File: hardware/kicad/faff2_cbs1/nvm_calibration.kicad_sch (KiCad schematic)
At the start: 0 parts

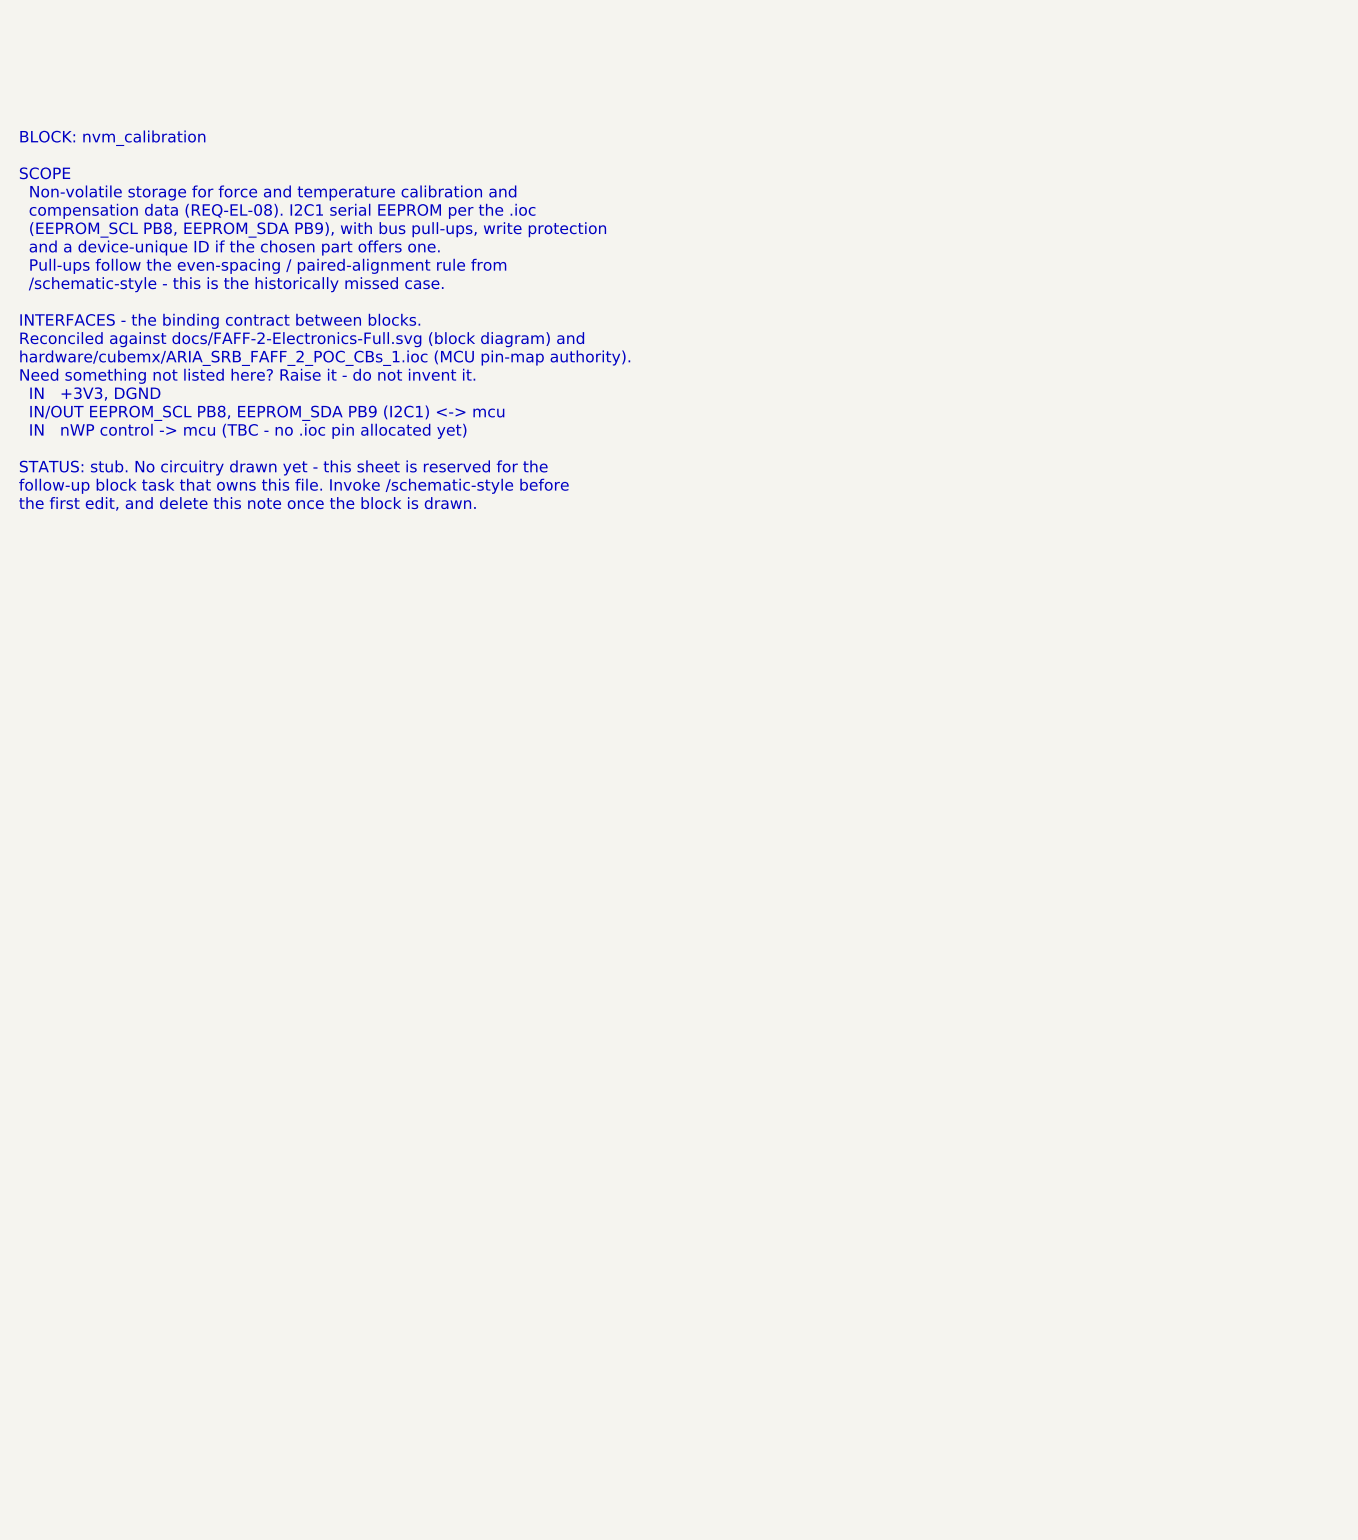
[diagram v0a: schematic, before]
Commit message: periph: draw linear_encoder, nvm_calibration and ui_io
Three peripheral block sheets for FAFF 2 CBs_1, drawn to the
/schematic-style house rules on the KiCad 9 A3 frame.

linear_encoder (REQ-PS-01..10, REQ-AR-07, DEC-0003)
  Bogen IKP11-Z1.4-P1-V5-D1-R0.5-F1000-C1 read head on two parallel
  connectors - a 10-way 0.5 mm FFC (J601, the stock Bogen cable) and a
  2x5 1.27 mm header (J602, the REQ-PS-09 alternative and the quadrature
  injection point).  AM26LV32 quad RS-422 receiver on 3V3 gives native
  3V3 outputs into TIM5; 120 R per pair, with a mid-rail reference and
  three links that switch the block to single-ended / TTL for a D3 head
  or bench injection.  Filtered 5 V read-head supply with its own
  current break, and test points on the receiver outputs.

nvm_calibration (REQ-EL-08, REQ-AR-11)
  24FC16T-I/OT 16 kbit I2C EEPROM on I2C1, 4k7 pull-ups on removable
  links, in-line solder bridges to take the device off the bus, and a
  write-protect network that resolves OQ-06 without spending an MCU pin.

ui_io (REQ-EL-05/06/09, REQ-CC-06, REQ-SF-01/02/05, DEC-0012)
  Status LEDs, two buttons with an external-button connector for the
  REQ-CC-06 homing trigger, a buffered 50 ohm source-terminated SMA
  SYNC output from TIM15_CH1, and normally-closed end-of-stroke limit
  switches whose two healthy-limit nodes are ANDed into LIMIT_nBRK for
  the TIM1_BKIN2 hardware kill.

References are allocated per sheet from the root page number (6xx, 8xx,
9xx) so the parallel block sheets cannot collide.

Datasheets fetched and committed for the parts selected here.

Co-Authored-By: Claude Opus 5 <noreply@anthropic.com>
Claude-Session: https://claude.ai/code/session_01BewsoRxMKiykAUhQw3HtBp
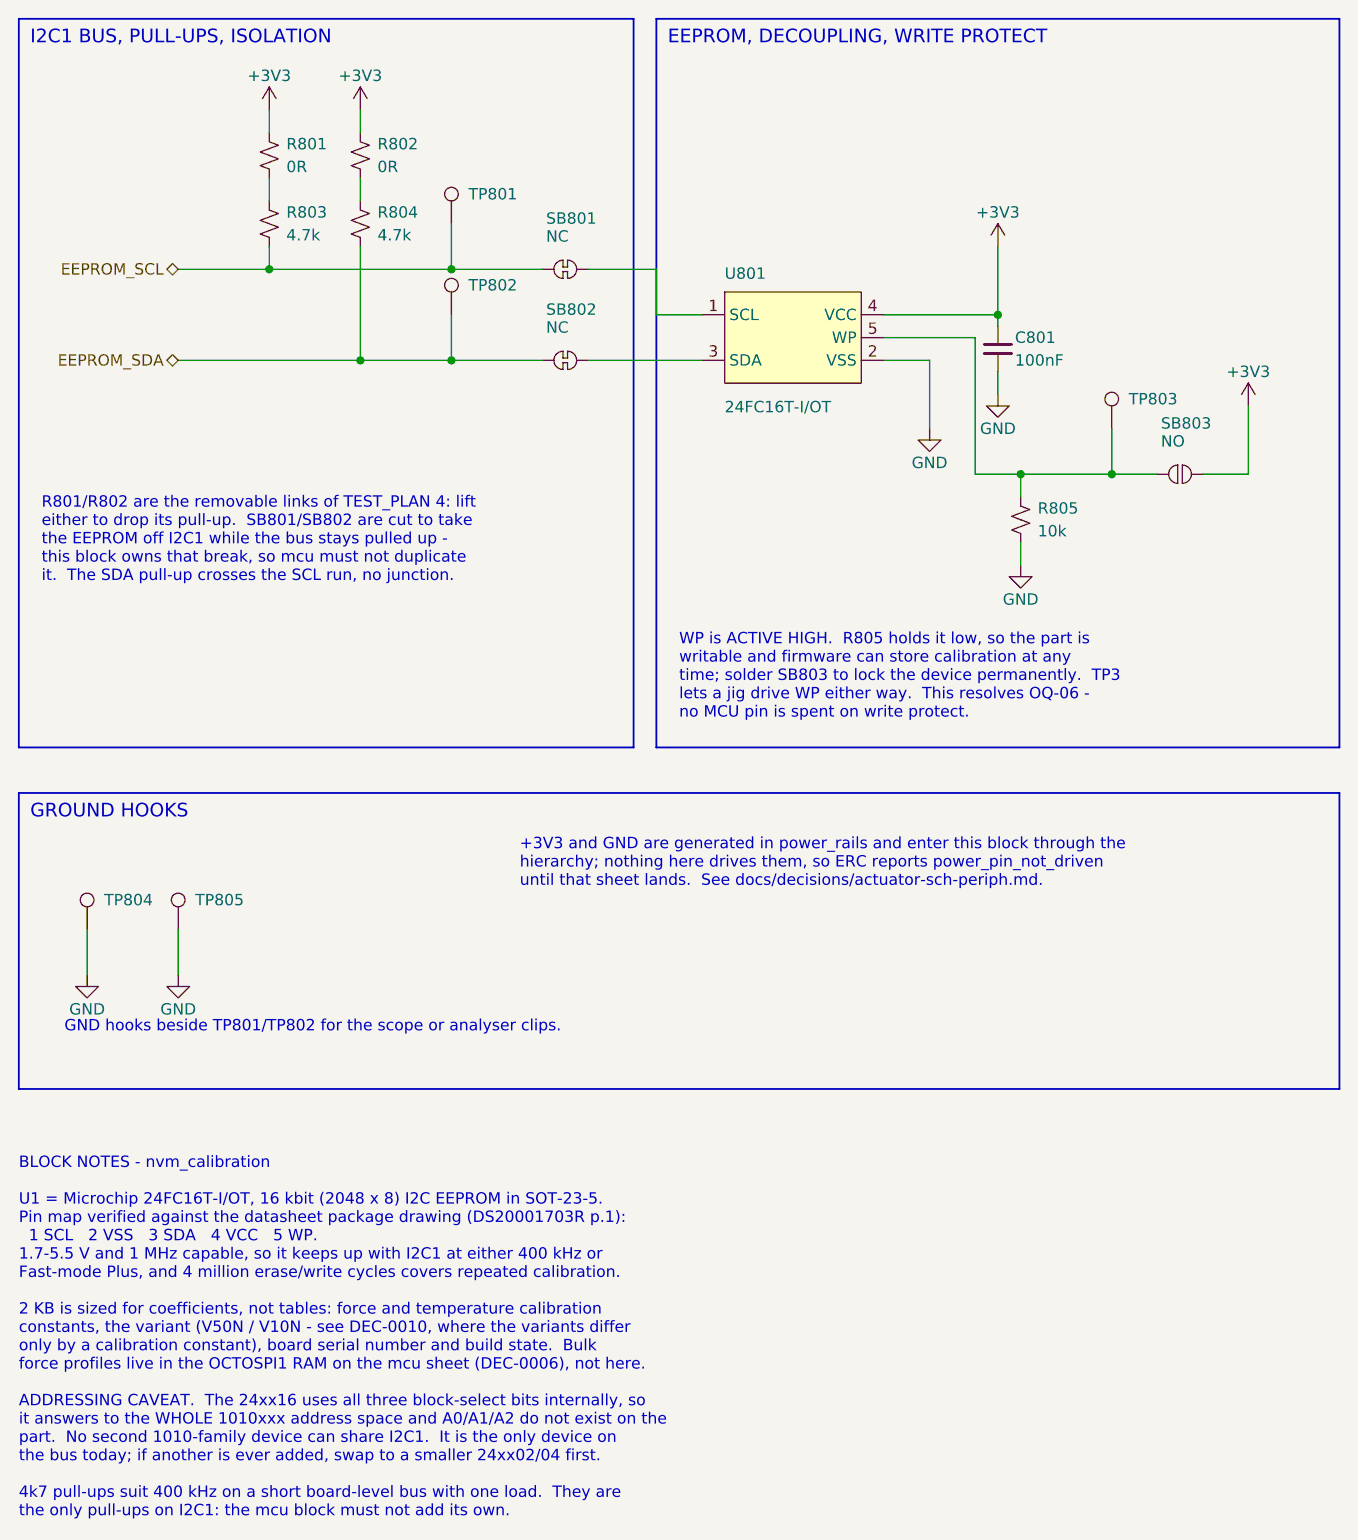
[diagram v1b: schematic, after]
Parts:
- added C801: 100nF, Amodo:C_0603_1608Metric, symbol Amodo_Capacitors:CAP_MLCC_100nF_0603_20%_50V
- added R801, R802: 0R, Amodo:R_0603_1608Metric, symbol Amodo_Resistors:RES_TF_0R_0603
- added R803, R804: 4.7k, Amodo:R_0603_1608Metric, symbol Amodo_Resistors:RES_TF_4.7k_0603
- added R805: 10k, Amodo:R_0603_1608Metric, symbol Amodo_Resistors:RES_TF_10k_0603
- added SB801, SB802: NC, Amodo:SOLDER_JUMPER_NC, symbol Amodo_Resistors:JUMPER_SOLDERABLE_NC
- added SB803: NO, Amodo:SOLDER_JUMPER_NO, symbol Amodo_Resistors:JUMPER_SOLDERABLE_NO
- added TP801, TP802, TP804, TP805: TestPoint, Amodo:KeystoneMiniatureTestLoop, symbol Amodo_Connectors:TestPointHook
- added TP803: TestPoint, Amodo:TestPoint_Pad_D1.0mm, symbol Amodo_Connectors:TestPoint
- added U801: 24FC16T-I/OT, Amodo:SOT23-5 - TI, symbol Amodo_Digital_ICs:24FC16T-I/OT
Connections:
- new net: R805.1, SB803.1, TP803.1, U801.5 (WP)
- new net: R802.2, R804.1
- new net: SB801.2, U801.1 (SCL)
- new net: SB802.2, U801.3 (SDA)
- new net: R801.2, R803.1
- new net +3V3: C801.1, R801.1, R802.1, SB803.2, U801.4 (VCC)
- new net EEPROM_SCL: R803.2, SB801.1, TP801.1
- new net EEPROM_SDA: R804.2, SB802.1, TP802.1
- new net GND: C801.2, R805.2, TP804.1, TP805.1, U801.2 (VSS)
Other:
- note added: "+3V3 and GND are generated in power_rails and enter this block through the hierarchy; nothing here drives them, so ERC reports power_pin_not_driven until that sheet lands. See docs/decisions/actuator-sch-periph.md."
- note added: "BLOCK NOTES - nvm_calibration U1 = Microchip 24FC16T-I/OT, 16 kbit (2048 x 8) I2C EEPROM in SOT-23-5. Pin map verified against the datasheet package drawing (DS20001703R p.1): 1 SCL 2 VSS 3 SDA 4 VCC 5 WP. 1.7-5.5 V and 1 MHz capable, so it keeps up with I2C1 at either 400 kHz or Fast-mode Plus, and 4 million erase/write cycles covers repeated calibration. 2 KB is sized for coefficients, not tabl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"
- note added: "EEPROM, DECOUPLING, WRITE PROTECT"
- note added: "GND hooks beside TP801/TP802 for the scope or analyser clips."
- note added: "GROUND HOOKS"
- note added: "I2C1 BUS, PULL-UPS, ISOLATION"
- note added: "R801/R802 are the removable links of TEST_PLAN 4: lift either to drop its pull-up. SB801/SB802 are cut to take the EEPROM off I2C1 while the bus stays pulled up - this block owns that break, so mcu must not duplicate it. The SDA pull-up crosses the SCL run, no junction."
- note added: "WP is ACTIVE HIGH. R805 holds it low, so the part is writable and firmware can store calibration at any time; solder SB803 to lock the device permanently. TP3 lets a jig drive WP either way. This resolves OQ-06 - no MCU pin is spent on write protect."
- note removed: "BLOCK: nvm_calibration SCOPE Non-volatile storage for force and temperature calibration and compensation data (REQ-EL-08). I2C1 serial EEPROM per the .ioc (EEPROM_SCL PB8, EEPROM_SDA PB9), with bus pull-ups, write protection and a device-unique ID if the chosen part offers one. Pull-ups follow the even-spacing / paired-alignment rule from /schematic-style - this is the historically missed case. I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"

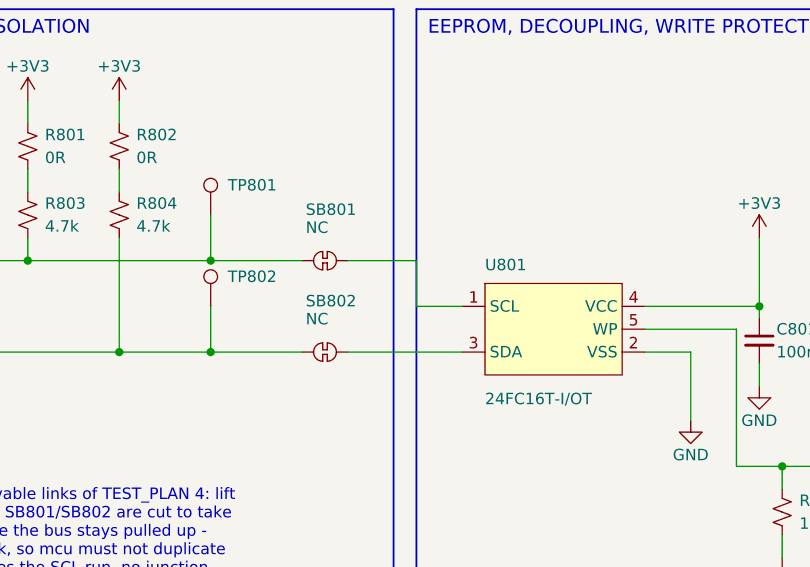
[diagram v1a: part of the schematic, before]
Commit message: review r1: logic-analyser headers, U501 reference note, AFE/encoder fixes
Answers the captain's round-1 review points on loadcell_afe, linear_encoder,
temp_sense and nvm_calibration.

U501 and the reference (R1). The ADS1235 has no internal reference and no
reference output pin - REFP0/REFN0 are inputs. The reference is the load cell's
own excitation, sensed at the bridge, which is what makes the measurement
ratiometric. Documented in a 15-line note beside U501B's reference pins.

Logic-analyser headers (R2, R5). The Amodo keyed 10-way 0.1in socket
(8510-4500PL) replaces the per-net hooks:

  J502  loadcell_afe   CH0..CH7 = the whole SPI3 interface plus nDRDY, START,
                       nRESET and CLKIN; TP506..TP512 and TP514 removed
  J603  linear_encoder CH0..CH4 = the three receiver outputs plus ENC_SDO and
                       ENC_nPROG; TP602..TP607 removed

Both tap the driver side of the series terminators, so the header still sees the
bus when an isolation link is lifted. J602 is KEPT: it carries REQ-PS-09, its
pin 9 is +5V_ENC where the socket wants GND, and six of its signals are the
terminated RS-422 pairs that DEC-0018 ruling 1 keeps stub-free. Raised as a
decision; ruled option (a) and captain-ratified.

J601 (R3, R4). Reference text moved off the body; the project-local
FH12-10S-0.5SH(55) symbol now shows pin numbers and names every pin (1..10,
MP1/MP2), matching the FH35C house exemplar. Fixed in faff2_periph.kicad_sym
and in the sheet's embedded copy, so no lib_symbol_mismatch.

5 V read-head supply (R6). R608, R609 and D602 are DNP parallel positions on
R601, FB601 and D601. Not for current sharing - the ferrite alone has 4x margin
on the CALC budget - but for bring-up: a shunt at R608 meters head current in
circuit, R609 bypasses the bead, D602 is a second SC-79 clamp. Moving D601 up
to make room also cleared its value text off the ENC_nPROG label and its ground
triangle off the ENC_nPROG wire.

temp_sense C701/C702 (R7). Both had their groun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
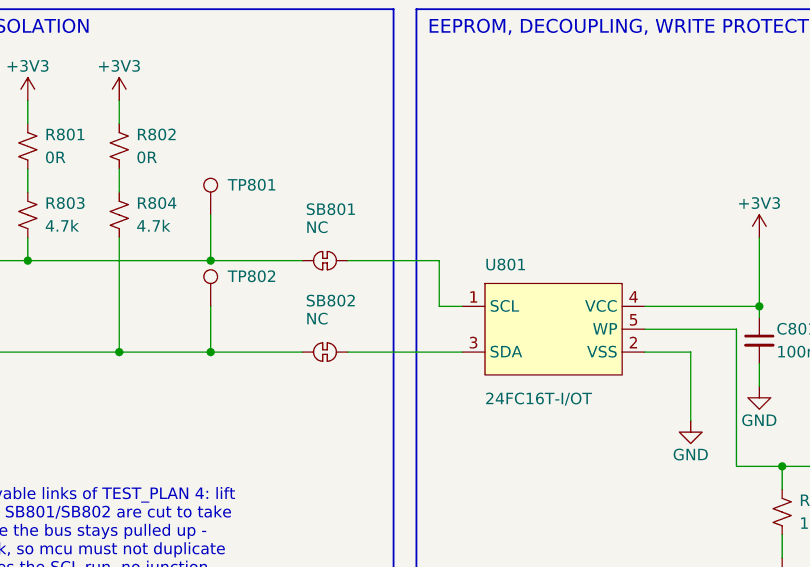
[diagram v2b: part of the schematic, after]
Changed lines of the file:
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@@
 	(wire
 		(pts
-			(xy 78.7400 40.6400) (xy 86.3600 40.6400)
+			(xy 78.7400 40.6400) (xy 88.9000 40.6400)
 		)
 		(stroke
@@
 	(wire
 		(pts
-			(xy 86.3600 40.6400) (xy 86.3600 45.7200)
+			(xy 88.9000 40.6400) (xy 88.9000 45.7200)
 		)
 		(stroke
@@
 	(wire
 		(pts
-			(xy 86.3600 45.7200) (xy 91.4400 45.7200)
+			(xy 88.9000 45.7200) (xy 91.4400 45.7200)
 		)
 		(stroke

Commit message: review r1 final sweep: power labels, TP silkscreen names, text overlaps
The captain's design-wide pass, run once the per-sheet batches had landed.
Presentation only: ERC 0 errors / 0 warnings at severity-all, 404 components,
251 nets, and every per-net node set identical to the pre-sweep export.

  power labels   92 rail names were hidden on loadcell_afe, motor_drive and
                 temp_sense - all 285 power symbols now read, placed to the
                 house pattern (GND below the symbol, rail arrows above)
  test points    66 of 83 still carried the library default "TestPoint". All
                 83 now name what they measure, from the net they actually
                 land on in the netlist; longest is 5 characters
  text overlap   16 collisions cleared design-wide, four of them sub-millimetre
                 ones the bundled checker passes because it under-measures text
  GND upside down  none - 0 of 285 power symbols is rotated or mirrored
  graphic/wire   one: power_rails block D's bottom border lay along the last
                 PWR_FLAG's wire; the flag column moved up 2.54

The overlap checker turns out to have three separable blind spots, each settled
here by measuring a render rather than by reading the format: it grows every
text field rightward regardless of justify/mirror/180-rotation, so its box is a
mirror image of the truth for those and it both invents and misses collisions;
it measures text at ~1.06 mm per character where the real advance is ~1.19; and
it reflects a rotated symbol's body about the origin. tools/sch_geom.py models
all three correctly and the design is clean under it design-wide. Two of that
model's own rules - notes growing up from their anchor, and labels taking no
180-degree justify flip - were bugs of mine that the checker caught first. The
render is what settles it; neither tool is authoritative alone.

Placement is searched rather than guessed: 177 newly visible fields are tried
against every wire, block border, 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
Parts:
- TP801: value TestPoint -> SCL
- TP802: value TestPoint -> SDA
- TP803: value TestPoint -> WP
- TP804, TP805: value TestPoint -> GND
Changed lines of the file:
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@@
 			)
 		)
-		(property "Value" "TestPoint"
-			(at 63.5000 30.4800 0)
-			(effects
-				(font
-					(size 1.27 1.27)
-				)
-				(hide yes)
+		(property "Value" "SCL"
+			(at 65.4 34.66 0)
+			(effects
+				(font
+					(size 1.27 1.27)
+				)
+				(justify left)
 			)
 		)
@@
 			)
 		)
-		(property "Value" "TestPoint"
-			(at 63.5000 40.6400 0)
-			(effects
-				(font
-					(size 1.27 1.27)
-				)
-				(hide yes)
+		(property "Value" "SDA"
+			(at 65.4 44.82 0)
+			(effects
+				(font
+					(size 1.27 1.27)
+				)
+				(justify left)
 			)
 		)
@@
 			)
 		)
-		(property "Value" "TestPoint"
-			(at 137.1600 53.3400 0)
-			(effects
-				(font
-					(size 1.27 1.27)
-				)
-				(hide yes)
+		(property "Value" "WP"
+			(at 139.06 57.52 0)
+			(effects
+				(font
+					(size 1.27 1.27)
+				)
+				(justify left)
 			)
 		)
@@
 			)
 		)
-		(property "Value" "TestPoint"
-			(at 22.8600 109.2200 0)
-			(effects
-				(font
-					(size 1.27 1.27)
-				)
-				(hide yes)
+		(property "Value" "GND"
+			(at 24.76 113.4 0)
+			(effects
+				(font
+					(size 1.27 1.27)
+				)
+				(justify left)
 			)
 		)
@@
 			)
 		)
-		(property "Value" "TestPoint"
-			(at 33.0200 109.2200 0)
-			(effects
-				(font
-					(size 1.27 1.27)
-				)
-				(hide yes)
-			)
-		)
+		(property "Value" "GND"
+			(at 34.92 113.4 0)
+			(effects
+				(font
+					(size 1.27 1.27)
+				)
+				(justify left)
+			)
+		)
